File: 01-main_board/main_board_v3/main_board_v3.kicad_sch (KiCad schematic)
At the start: 12 parts, among them J1 FFC to Main_Peripheral, J2 FFC Analog, J3 FFC Digital

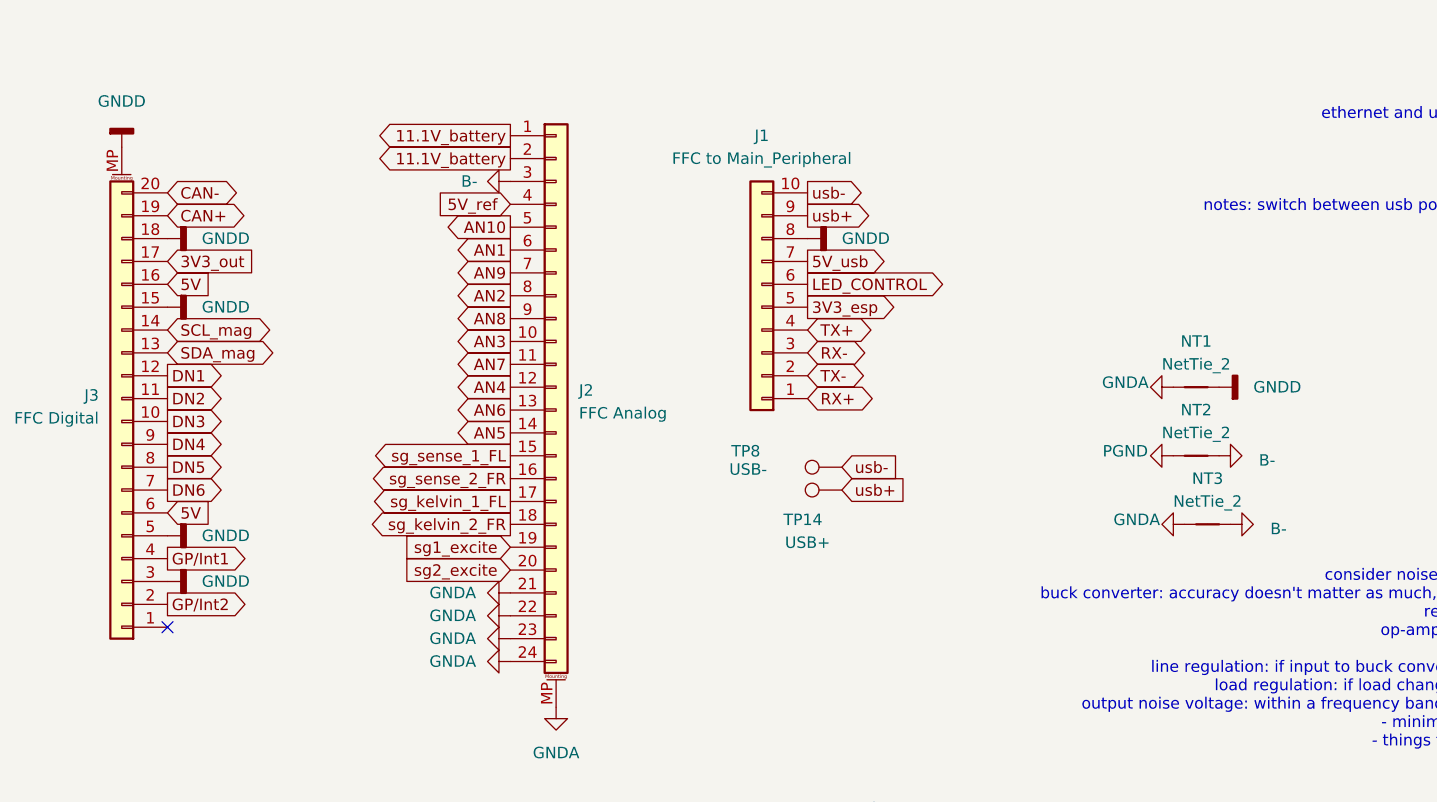
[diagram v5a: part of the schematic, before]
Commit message: changed peripheral connector, addressed slack revisions
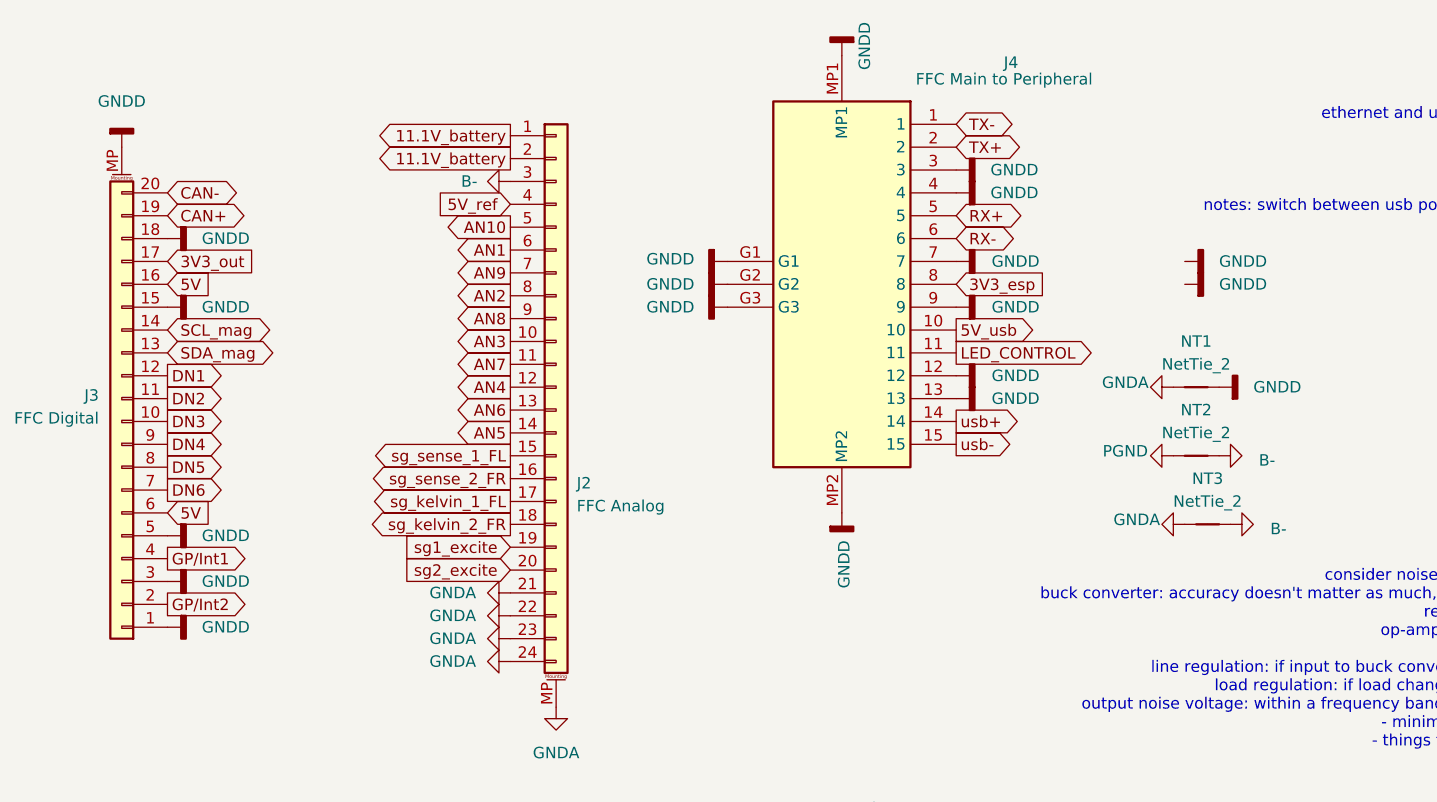
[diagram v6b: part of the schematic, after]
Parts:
- removed J1: FFC to Main_Peripheral, Connector_FFC-FPC:TE_1-84952-0_1x10-1MP_P1.0mm_Horizontal, symbol Connector_Generic:Conn_01x10
- removed TP14: USB+, TestPoint:TestPoint_Pad_D1.0mm, symbol Connector:TestPoint
- removed TP8: USB-, TestPoint:TestPoint_Pad_D1.0mm, symbol Connector:TestPoint
- added J4: FFC Main to Peripheral, 22XT_Main:FH4115S05SH05, symbol 22XT_Main_v2:FH41-15S-0.5SH_05_
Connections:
- net 3V3_esp: now also J4.8
- net 5V_usb: now also J4.10
- net GNDD: now also J3.1 (Pin_1), J4.12, J4.13, J4.3, J4.4, J4.7, J4.9, J4.G1, J4.G2, J4.G3, J4.MP1, J4.MP2
- net LED_CONTROL: now also J4.11
- net RX+: now also J4.5
- net RX-: now also J4.6
- net TX+: now also J4.2
- net TX-: now also J4.1
- net usb+: now also J4.14
- net usb-: now also J4.15
- no-connect marks 1 -> 0

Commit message: finished silkscreen + 3D models
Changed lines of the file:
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@@
-	(symbol
-		(lib_id "power:GNDD")
-		(at 184.15 44.45 90)
-		(unit 1)
-		(exclude_from_sim no)
-		(in_bom yes)
-		(on_board yes)
-		(dnp no)
-		(fields_autoplaced yes)
-		(property "Reference" "#PWR083"
-			(at 190.5 44.45 0)
-			(effects
-				(font
-					(size 1.27 1.27)
-				)
-				(hide yes)
-			)
-		)
-		(property "Value" "GNDD"
-			(at 187.96 44.4499 90)
-			(effects
-				(font
-					(size 1.27 1.27)
-				)
-				(justify right)
-			)
-		)
-		(property "Footprint" ""
-			(at 184.15 44.45 0)
-			(effects
-				(font
-					(size 1.27 1.27)
-				)
-				(hide yes)
-			)
-		)
-		(property "Datasheet" ""
-			(at 184.15 44.45 0)
-			(effects
-				(font
-					(size 1.27 1.27)
-				)
-				(hide yes)
-			)
-		)
-		(property "Description" "Power symbol creates a global label with name \"GNDD\" , digital ground"
-			(at 184.15 44.45 0)
-			(effects
-				(font
-					(size 1.27 1.27)
-				)
-				(hide yes)
-			)
-		)
-		(pin "1"
-		)
-		(instances
-			(project "main_board_v3"
-				(path "/12c2237c-5932-49af-9119-92b28c846ae7"
-					(reference "#PWR083")
-					(unit 1)
-				)
-			)
-		)
-	)
 	(symbol
 		(lib_id "power:GNDD")
@@
 					(unit 1)
 				)
-			)
-		)
-	)
-	(symbol
-		(lib_id "power:GNDD")
-		(at 184.15 41.91 90)
-		(unit 1)
-		(exclude_from_sim no)
-		(in_bom yes)
-		(on_board yes)
-		(dnp no)
-		(fields_autoplaced yes)
-		(property "Reference" "#PWR082"
-			(at 190.5 41.91 0)
-			(effects
-				(font
-					(size 1.27 1.27)
-				)
-				(hide yes)
-			)
-		)
-		(property "Value" "GNDD"
-			(at 187.96 41.9099 90)
-			(effects
-				(font
-					(size 1.27 1.27)
-				)
-				(justify right)
-			)
-		)
-		(property "Footprint" ""
-			(at 184.15 41.91 0)
-			(effects
-				(font
-					(size 1.27 1.27)
-				)
-				(hide yes)
-			)
-		)
-		(property "Datasheet" ""
-			(at 184.15 41.91 0)
-			(effects
-				(font
-					(size 1.27 1.27)
-				)
-				(hide yes)
-			)
-		)
-		(property "Description" "Power symbol creates a global label with name \"GNDD\" , digital ground"
-			(at 184.15 41.91 0)
-			(effects
-				(font
-					(size 1.27 1.27)
-				)
-				(hide yes)
-			)
-		)
-		(pin "1"
-		)
-		(instances
-			(project "main_board_v3"
-				(path "/12c2237c-5932-49af-9119-92b28c846ae7"
-					(reference "#PWR082")
-					(unit 1)
-				)

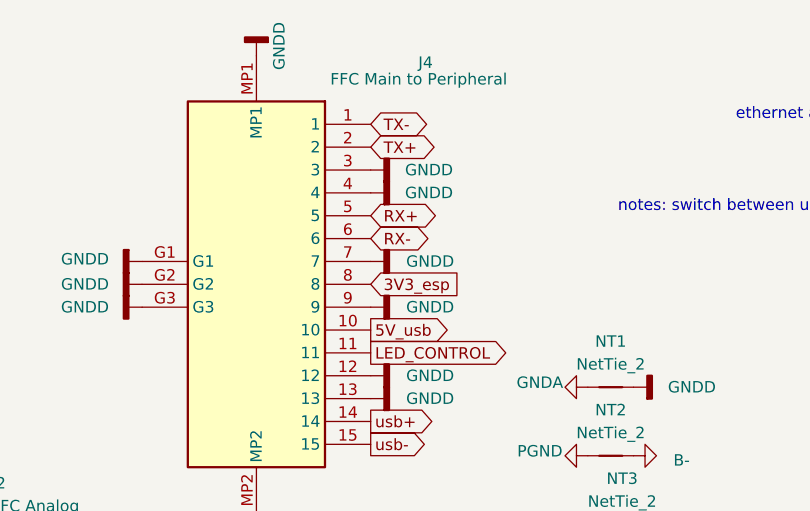
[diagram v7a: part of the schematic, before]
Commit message: moved down peripheral ffc connector by > 5 mm
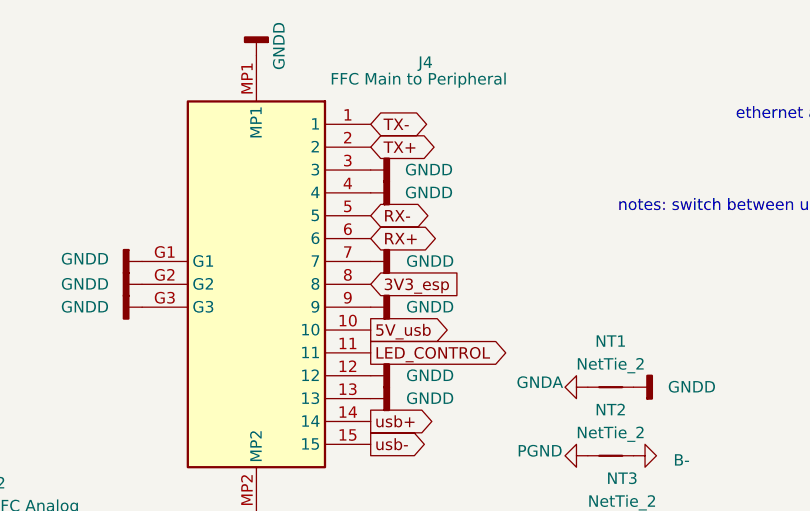
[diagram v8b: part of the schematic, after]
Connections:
- net RX+: now also J4.6; no longer J4.5
- net RX-: now also J4.5; no longer J4.6
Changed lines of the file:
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@@
+		)
+	)
+	(global_label "RX-"
+		(shape bidirectional)
+		(at 158.75 36.83 0)
+		(fields_autoplaced yes)
+		(effects
+			(font
+				(size 1.27 1.27)
+			)
+			(justify left)
+		)
+		(property "Intersheetrefs" "${INTERSHEET_REFS}"
+			(at 166.8984 36.83 0)
+			(effects
+				(font
+					(size 1.27 1.27)
+				)
+				(justify left)
+				(hide yes)
+			)
 		)
 	)
@@
 		)
 	)
-	(global_label "RX-"
-		(shape bidirectional)
-		(at 158.75 39.37 0)
-		(fields_autoplaced yes)
-		(effects
-			(font
-				(size 1.27 1.27)
-			)
-			(justify left)
-		)
-		(property "Intersheetrefs" "${INTERSHEET_REFS}"
-			(at 166.8984 39.37 0)
-			(effects
-				(font
-					(size 1.27 1.27)
-				)
-				(justify left)
-				(hide yes)
-			)
-		)
-	)
 	(global_label "AN1"
 		(shape input)
@@
 		)
 	)
-	(global_label "hallfx_4_FL"
-		(shape output)
-		(at 36.83 69.85 180)
-		(fields_autoplaced yes)
-		(effects
-			(font
-				(face "KiCad Font")
-				(size 1.27 1.27)
-			)
-			(justify right)
-		)
-		(property "Intersheetrefs" "${INTERSHEET_REFS}"
-			(at 23.2012 69.85 0)
-			(effects
-				(font
-					(size 1.27 1.27)
-				)
-				(justify right)
-				(hide yes)
-			)
-		)
-	)
 	(global_label "RX+"
 		(shape bidirectional)
-		(at 158.75 36.83 0)
-		(fields_autoplaced yes)
-		(effects
-			(font
-				(size 1.27 1.27)
-			)
-			(justify left)
-		)
-		(property "Intersheetrefs" "${INTERSHEET_REFS}"
-			(at 166.8984 36.83 0)
-			(effects
-				(font
-					(size 1.27 1.27)
-				)
-				(justify left)
-				(hide yes)
-			)
+		(at 158.75 39.37 0)
+		(fields_autoplaced yes)
+		(effects
+			(font
+				(size 1.27 1.27)
+			)
+			(justify left)
+		)
+		(property "Intersheetrefs" "${INTERSHEET_REFS}"
+			(at 166.8984 39.37 0)
+			(effects
+				(font
+					(size 1.27 1.27)
+				)
+				(justify left)
+				(hide yes)
+			)
+		)
+	)
+	(global_label "hallfx_4_FL"
+		(shape output)
+		(at 36.83 69.85 180)
+		(fields_autoplaced yes)
+		(effects
+			(font
+				(face "KiCad Font")
+				(size 1.27 1.27)
+			)
+			(justify right)
+		)
+		(property "Intersheetrefs" "${INTERSHEET_REFS}"
+			(at 23.2012 69.85 0)
+			(effects
+				(font
+					(size 1.27 1.27)
+				)
+				(justify right)
+				(hide yes)
+			)
